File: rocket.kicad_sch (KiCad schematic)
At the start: 33 parts, among them SW1 SW_SPST, U1 MCP6L04T-E_SL, U2 Teensy4.1

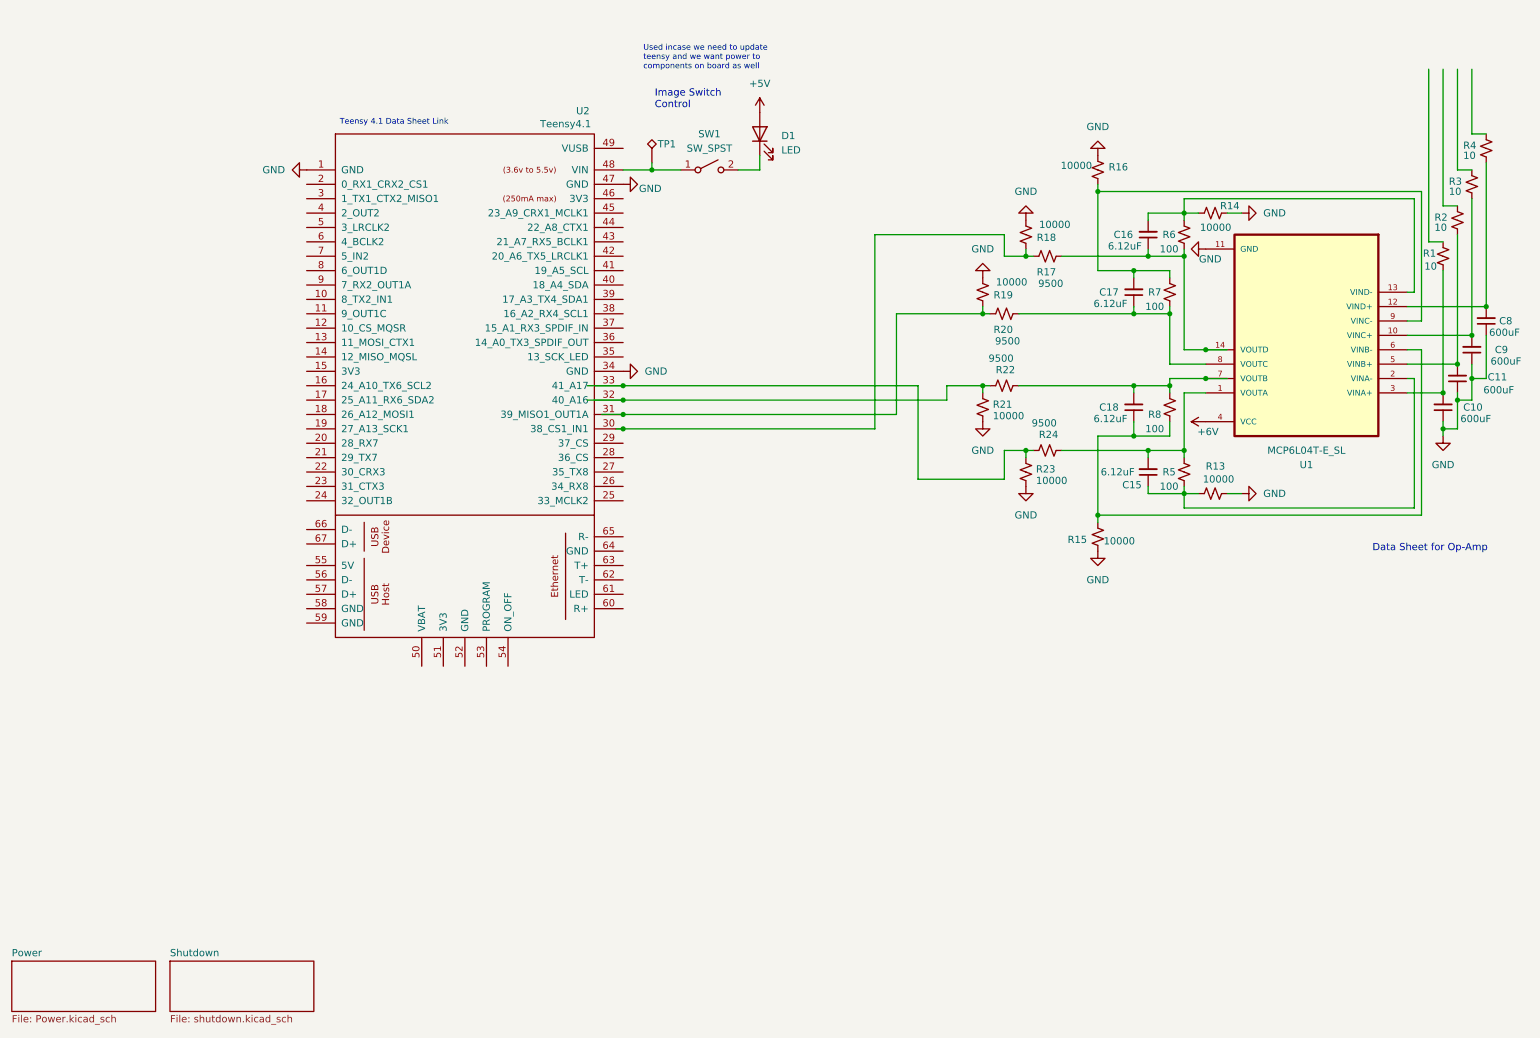
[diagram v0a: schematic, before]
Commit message: SDC Creation & Cleanup
*Created Title Page with notes for schematic
*Created SDC (INCOMPLETE)
*Cleaned up input buffer schem
*New component numbering convention
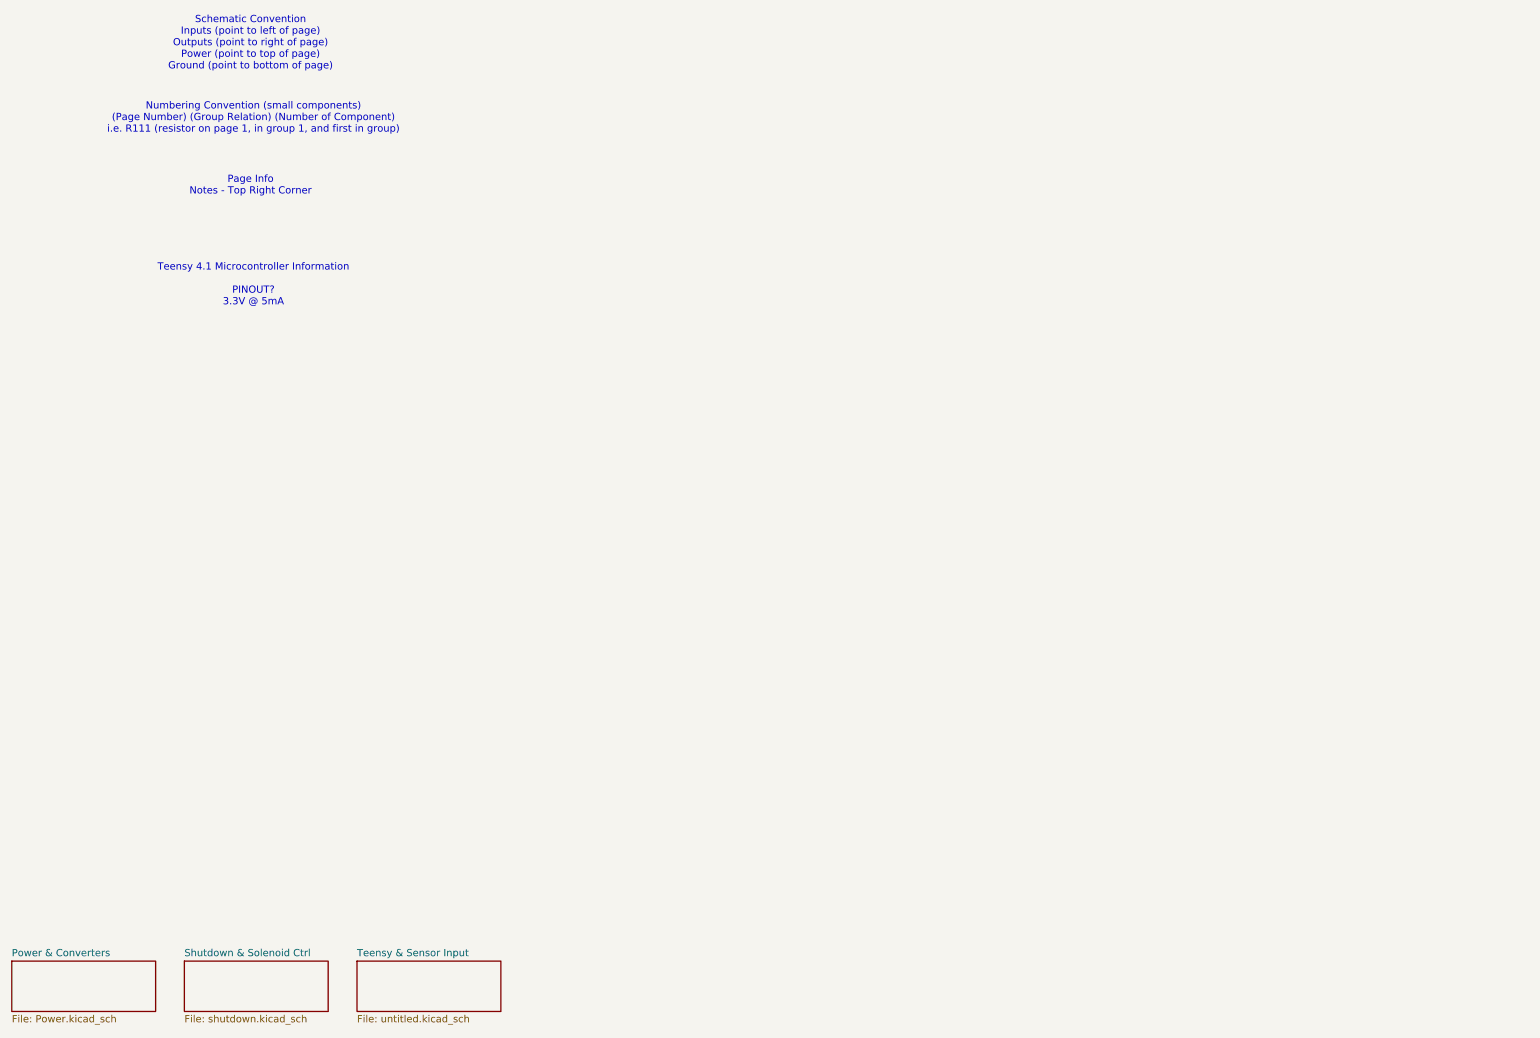
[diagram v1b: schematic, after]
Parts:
- removed C10, C11, C8, C9: 600uF, symbol Device:C_Small
- removed C15, C16, C17, C18: 6.12uF, symbol Device:C_Small
- removed D1: LED, symbol Device:LED
- removed R1, R2, R3, R4: 10, symbol Device:R_Small_US
- removed R13, R14, R15, R16, R18, R19, R21, R23: 10000, symbol Device:R_Small_US
- removed R17, R20, R22, R24: 9500, symbol Device:R_Small_US
- removed R5, R6, R7, R8: 100, symbol Device:R_Small_US
- removed SW1: SW_SPST, symbol Switch:SW_SPST
- removed TP1: TestPoint_Alt, symbol Connector:TestPoint_Alt
- removed U1: MCP6L04T-E_SL, MCP6L04T-E_SL:SOIC127P600X175-14N, symbol MCP6L04T-E_SL:MCP6L04T-E_SL
- removed U2: Teensy4.1, symbol teensy:Teensy4.1
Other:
- sheet Power renamed Power & Converters
- sheet Shutdown renamed Shutdown & Solenoid Ctrl
- added sheet Teensy & Sensor Input (untitled.kicad_sch)
- note added: "Numbering Convention (small components) (Page Number) (Group Relation) (Number of Component) i.e. R111 (resistor on page 1, in group 1, and first in group)"
- note added: "Page Info Notes - Top Right Corner"
- note added: "Schematic Convention Inputs (point to left of page) Outputs (point to right of page) Power (point to top of page) Ground (point to bottom of page)"
- note added: "Teensy 4.1 Microcontroller Information PINOUT? 3.3V @ 5mA"
- note removed: "Data Sheet for Op-Amp"
- note removed: "Image Switch Control"
- note removed: "Teensy 4.1 Data Sheet Link"
- note removed: "Used incase we need to update teensy and we want power to components on board as well"
- title: Controller -> General Information
